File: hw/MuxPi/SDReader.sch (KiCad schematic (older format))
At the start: 32 parts, among them IC1 AT24C02D-SSHM-T, P17 USBA-2G, U9 USB2640-HZH-02, Y2 LF XTAL012504 - 24MHz

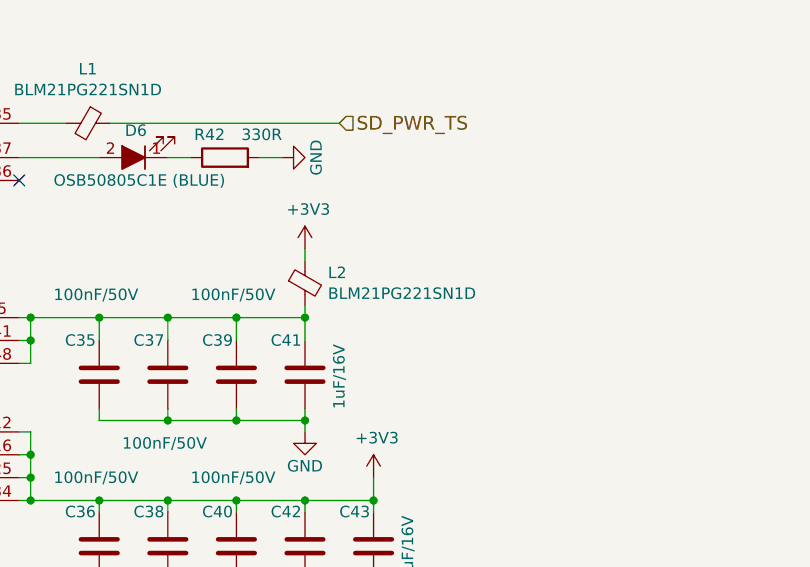
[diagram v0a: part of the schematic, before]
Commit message: Add detailed info to MuxPi electronic components
The additional information includes manufacturer names and
manufacturer symbols for all components except ceramic capacitors
and resistors. It allows to create BOM (Bill Of Materials) with
actual product names.

Change-Id: Id1c518bba60322d4b8b132ad14261806070abc27
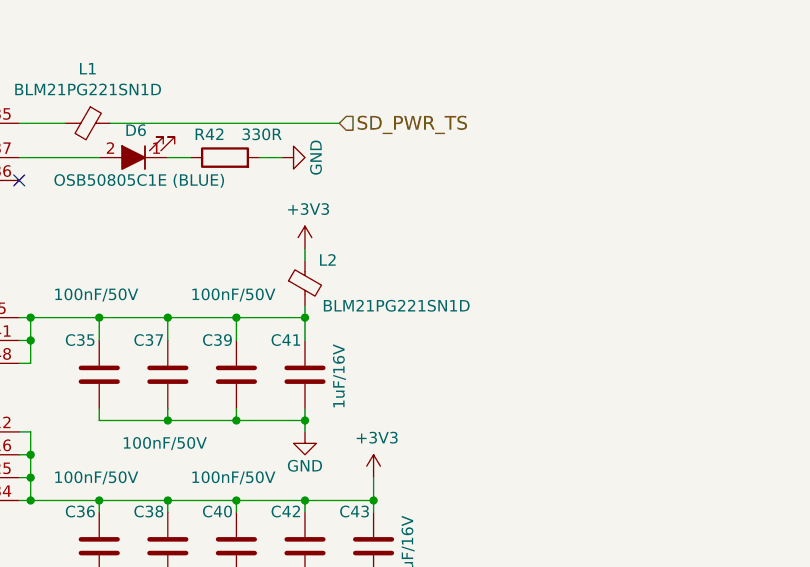
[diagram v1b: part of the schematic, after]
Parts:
- D6: Manufacturer (none) -> OPTOSUPPLY; Symbol (none) -> OSB50805C1E
- IC1: Manufacturer (none) -> MICROCHIP (ATMEL); Symbol (none) -> AT24C02D-SSHM-T
- L1, L2: Manufacturer (none) -> MURATA; Symbol (none) -> BLM21PG221SN1D
- P17: Manufacturer (none) -> CONNFLY; Symbol (none) -> DS1096-BN0
- U9: Manufacturer (none) -> MICROCHIP; Symbol (none) -> USB2640-HZH-02
- Y2: Manufacturer (none) -> IQD FREQUENCY PRODUCTS; Symbol (none) -> LF XTAL012504
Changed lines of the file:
@@
 F 3 "http://www.farnell.com/datasheets/2138035.pdf?_ga=1.187806955.291132730.1474618953" H 7450 2500 50  0001 C CNN
 F 4 "http://pl.farnell.com/microchip/usb2640-hzh-02/ic-usb-2-flash-media-cntrl-48vqfn/dp/2292611" H 5500 2400 60  0001 C CNN "Shop link"
+F 5 "USB2640-HZH-02" H 5500 2400 50  0001 C CNN "Symbol"
+F 6 "MICROCHIP" H 5500 2400 50  0001 C CNN "Manufacturer"
 	1    5500 2400
 	1    0    0    -1
@@
 F 3 "http://www.farnell.com/datasheets/2138035.pdf?_ga=1.187806955.291132730.1474618953" H 5250 6050 50  0001 C CNN
 F 4 "http://pl.farnell.com/microchip/usb2640-hzh-02/ic-usb-2-flash-media-cntrl-48vqfn/dp/2292611" H 3300 5950 60  0001 C CNN "Shop link"
+F 5 "MICROCHIP" H 3300 5950 50  0001 C CNN "Manufacturer"
+F 6 "USB2640-HZH-02" H 3300 5950 50  0001 C CNN "Symbol"
 	2    3300 5950
 	1    0    0    -1
@@
 F 3 "http://www.tme.eu/pl/Document/9ec5256b58bf67caf05d35a0814832e6/AT24C01D-MAHM-T.pdf" H 3650 3600 50  0001 C CNN
 F 4 "http://www.tme.eu/pl/details/at24c02d-sshm-t/pamieci-eeprom-szeregowe/atmel/" H 3650 3600 60  0001 C CNN "Shop link"
+F 5 "MICROCHIP (ATMEL)" H 3650 3600 50  0001 C CNN "Manufacturer"
+F 6 "AT24C02D-SSHM-T" H 3650 3600 50  0001 C CNN "Symbol"
 	1    3650 3600
 	1    0    0    -1
@@
 F 3 "http://www.tme.eu/pl/Document/fd32e3a1954dc23b6c626158f627af96/hc49_4hsmx.pdf" H 1750 5550 50  0001 C CNN
 F 4 "http://www.tme.eu/pl/details/24.00m-smdhc49r/rezonatory-kwarcowe-smd/iqd-frequency-products/lf-xtal012504/" V 1750 5550 60  0001 C CNN "Shop link"
+F 5 "IQD FREQUENCY PRODUCTS" V 1750 5550 50  0001 C CNN "Manufacturer"
+F 6 "LF XTAL012504" V 1750 5550 50  0001 C CNN "Symbol"
 	1    1750 5550
 	0    1    1    0
@@
 $EndComp
 $Comp
-L MuxPi:Ferrite_Bead_Small L2
-U 1 1 5846AD7D
-P 5350 5900
-F 0 "L2" H 5450 5946 50  0000 L CNN
-F 1 "BLM21PG221SN1D" H 5450 5855 50  0000 L CNN
-F 2 "Resistors_SMD:R_0805_HandSoldering" H 5450 5809 50  0001 L CNN
-F 3 "http://www.tme.eu/pl/Document/6052c7f9d4f1672121538e0d10f79ff8/blm21pg300sn1d.pdf" H 5450 5809 50  0001 L CNN
-F 4 "http://www.tme.eu/pl/details/blm21pg221sn1d/ferryty-koraliki/murata/" H 5350 5900 60  0001 C CNN "Shop link"
-	1    5350 5900
-	1    0    0    -1
-$EndComp
-$Comp
 L MuxPi:+3V3 #PWR0129
 U 1 1 5846B688
@@
 F 3 "http://www.tme.eu/pl/Document/6052c7f9d4f1672121538e0d10f79ff8/blm21pg300sn1d.pdf" H 4500 5109 50  0001 L CNN
 F 4 "http://www.tme.eu/pl/details/blm21pg221sn1d/ferryty-koraliki/murata/" H 4400 5200 60  0001 C CNN "Shop link"
+F 5 "MURATA" V 4400 5200 50  0001 C CNN "Manufacturer"
+F 6 "BLM21PG221SN1D" V 4400 5200 50  0001 C CNN "Symbol"
 	1    4400 5200
 	0    1    1    0
@@
 F 3 "http://www.tme.eu/pl/Document/7923e8726ae07a0825304f6fd9a186c2/usba-2g.pdf" V 10350 1300 50  0001 C CNN
 F 4 "http://www.tme.eu/pl/details/usba-2g/zlacza-usb-i-ieee1394/ninigi/" V 10400 1400 60  0001 C CNN "Shop link"
+F 5 "CONNFLY" V 10400 1400 50  0001 C CNN "Manufacturer"
+F 6 "DS1096-BN0" V 10400 1400 50  0001 C CNN "Symbol"
 	1    10400 1400
 	0    1    1    0
@@
 F 3 "http://www.tme.eu/pl/Document/6f99baddc8b38eb1a865ea6b78250b2b/OSXX0805C1E-DTE.pdf" H 4600 5350 50  0001 C CNN
 F 4 "http://www.tme.eu/pl/details/osb50805c1e/diody-led-smd-kolorowe/optosupply/" V 4600 5350 60  0001 C CNN "Shop link"
+F 5 "OPTOSUPPLY" H 4600 5350 50  0001 C CNN "Manufacturer"
+F 6 "OSB50805C1E" H 4600 5350 50  0001 C CNN "Symbol"
 	1    4600 5350
 	-1   0    0    1
@@
 Wire Wire Line
 	1450 5800 1750 5800
+$Comp
+L MuxPi:Ferrite_Bead_Small L2
+U 1 1 5A8DBC88
+P 5350 5900
+F 0 "L2" H 5450 6000 50  0000 C CNN
+F 1 "BLM21PG221SN1D" H 5750 5800 50  0000 C CNN
+F 2 "Resistors_SMD:R_0805_HandSoldering" H 5450 5809 50  0001 L CNN
+F 3 "http://www.tme.eu/pl/Document/6052c7f9d4f1672121538e0d10f79ff8/blm21pg300sn1d.pdf" H 5450 5809 50  0001 L CNN
+F 4 "http://www.tme.eu/pl/details/blm21pg221sn1d/ferryty-koraliki/murata/" H 5350 5900 60  0001 C CNN "Shop link"
+F 5 "MURATA" V 5350 5900 50  0001 C CNN "Manufacturer"
+F 6 "BLM21PG221SN1D" V 5350 5900 50  0001 C CNN "Symbol"
+	1    5350 5900
+	1    0    0    -1
+$EndComp
 $EndSCHEMATC

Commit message: Update hardware design to version 1.3
Change-Id: I17b3f32943a6fd048f05d1b0d8676607dc54b976
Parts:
- L1, L2: footprint Resistors_SMD:R_0805_HandSoldering -> Resistors_SMD:R_0805
- R42: value 330R -> 560R; Shop link http://www.tme.eu/pl/details/rc0805jr-07330r/rezystory-smd-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 -> (none)
- R43: value 330R -> 10K; Shop link http://www.tme.eu/pl/details/rc0805jr-07330r/rezystory-smd-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 -> (none)
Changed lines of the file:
@@
 Sheet 9 12
 Title "MuxPi"
-Date "2018-04-20"
-Rev "1.2"
+Date "2018-08-14"
+Rev "1.3"
 Comp "SRPOL"
 Comment1 "Author: Adam Malinowski <a.malinowsk2@partner.samsung.com>"
-Comment2 "Copyright (c) 2016 - 2018 Samsung Electronics Co., Ltd All Rights Reserved"
+Comment2 "Copyright (c) 2016 -2018 Samsung Electronics Co., Ltd All Rights Reserved"
 Comment3 ""
 Comment4 ""
@@
 F 0 "L1" V 4163 5200 50  0000 C CNN
 F 1 "BLM21PG221SN1D" V 4254 5200 50  0000 C CNN
-F 2 "Resistors_SMD:R_0805_HandSoldering" H 4500 5109 50  0001 L CNN
+F 2 "Resistors_SMD:R_0805" H 4500 5109 50  0001 L CNN
 F 3 "http://www.tme.eu/pl/Document/6052c7f9d4f1672121538e0d10f79ff8/blm21pg300sn1d.pdf" H 4500 5109 50  0001 L CNN
 F 4 "http://www.tme.eu/pl/details/blm21pg221sn1d/ferryty-koraliki/murata/" H 4400 5200 60  0001 C CNN "Shop link"
@@
 P 5000 5350
 F 0 "R42" V 5100 5350 50  0000 L CNN
-F 1 "330R" V 5100 5100 50  0000 L CNN
+F 1 "560R" V 5100 5100 50  0000 L CNN
 F 2 "Resistors_SMD:R_0805" V 4930 5350 50  0001 C CNN
 F 3 "http://www.tme.eu/pl/Document/7b8fed8c112f8a94930279c22c957f7f/rc0805yageo.pdf" H 5000 5350 50  0001 C CNN
-F 4 "http://www.tme.eu/pl/details/rc0805jr-07330r/rezystory-smd-0805/yageo/rc0805jr-07330rl/" V 5000 5350 60  0001 C CNN "Shop link"
 	1    5000 5350
 	0    -1   -1   0
@@
 P 10600 2350
 F 0 "R43" H 10650 2450 50  0000 L CNN
-F 1 "330R" H 10650 2350 50  0000 L CNN
+F 1 "10K" H 10650 2350 50  0000 L CNN
 F 2 "Resistors_SMD:R_0805" V 10530 2350 50  0001 C CNN
 F 3 "http://www.tme.eu/pl/Document/7b8fed8c112f8a94930279c22c957f7f/rc0805yageo.pdf" H 10600 2350 50  0001 C CNN
-F 4 "http://www.tme.eu/pl/details/rc0805jr-07330r/rezystory-smd-0805/yageo/rc0805jr-07330rl/" V 10600 2350 60  0001 C CNN "Shop link"
 	1    10600 2350
 	1    0    0    -1
@@
 F 0 "L2" H 5450 6000 50  0000 C CNN
 F 1 "BLM21PG221SN1D" H 5750 5800 50  0000 C CNN
-F 2 "Resistors_SMD:R_0805_HandSoldering" H 5450 5809 50  0001 L CNN
+F 2 "Resistors_SMD:R_0805" H 5450 5809 50  0001 L CNN
 F 3 "http://www.tme.eu/pl/Document/6052c7f9d4f1672121538e0d10f79ff8/blm21pg300sn1d.pdf" H 5450 5809 50  0001 L CNN
 F 4 "http://www.tme.eu/pl/details/blm21pg221sn1d/ferryty-koraliki/murata/" H 5350 5900 60  0001 C CNN "Shop link"

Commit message: Update  hardware design to version 1.4
Change-Id: I72a4381d8bec5616bc1cfe04dc8a5407141c77d5
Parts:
- removed Y2: LF XTAL012504 - 24MHz, Crystals:Q_49U3HMS, symbol MuxPi:Crystal
- added Y2: LF XTAL012504 - 24MHz, Crystal:Crystal_SMD_2520-4Pin_2.5x2.0mm, symbol Device:Crystal_GND24
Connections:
- net GND: now also Y2.2, Y2.4
- net at C29.1, R37.2, U9.45 (XTAL1/CLKIN): now also Y2.1
- net at C30.1, R37.1, U9.44 (XTAL2): now also Y2.3
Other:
- moved on the sheet: R37
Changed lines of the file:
@@
 EESchema Schematic File Version 4
 LIBS:MuxPi-cache
-EELAYER 26 0
+EELAYER 29 0
 EELAYER END
 $Descr A4 11693 8268
@@
 Sheet 9 12
 Title "MuxPi"
-Date "2018-08-14"
-Rev "1.3"
+Date "2018-11-16"
+Rev "1.4"
 Comp "SRPOL"
 Comment1 "Author: Adam Malinowski <a.malinowsk2@partner.samsung.com>"
@@
 $EndComp
 $Comp
-L MuxPi:Crystal Y2
-U 1 1 584578D0
-P 1750 5550
-F 0 "Y2" V 1600 5450 50  0000 C CNN
-F 1 "LF XTAL012504 - 24MHz" V 1350 5800 50  0000 C CNN
-F 2 "Crystals:Q_49U3HMS" H 1750 5550 50  0001 C CNN
-F 3 "http://www.tme.eu/pl/Document/fd32e3a1954dc23b6c626158f627af96/hc49_4hsmx.pdf" H 1750 5550 50  0001 C CNN
-F 4 "http://www.tme.eu/pl/details/24.00m-smdhc49r/rezonatory-kwarcowe-smd/iqd-frequency-products/lf-xtal012504/" V 1750 5550 60  0001 C CNN "Shop link"
-F 5 "IQD FREQUENCY PRODUCTS" V 1750 5550 50  0001 C CNN "Manufacturer"
-F 6 "LF XTAL012504" V 1750 5550 50  0001 C CNN "Symbol"
-	1    1750 5550
-	0    1    1    0
-$EndComp
-$Comp
 L MuxPi:GND #PWR0121
 U 1 1 584578D7
@@
 	2150 5750 2100 5750
 Wire Wire Line
-	2100 5350 2100 5750
+	2100 5350 2100 5550
 Wire Wire Line
 	850  5800 950  5800
@@
 	850  5300 950  5300
 Wire Wire Line
-	1250 5300 1450 5300
-Wire Wire Line
-	1250 5800 1450 5800
+	1250 5300 1350 5300
+Wire Wire Line
+	1250 5800 1350 5800
 Wire Wire Line
 	1750 5400 1750 5300
@@
 Connection ~ 1750 5800
 Wire Wire Line
-	2500 5500 1950 5500
-Wire Wire Line
-	1950 5500 1950 5300
-Wire Wire Line
-	2500 5600 1950 5600
-Wire Wire Line
-	1950 5600 1950 5800
+	2500 5500 2000 5500
+Wire Wire Line
+	2000 5500 2000 5300
+Wire Wire Line
+	2500 5600 2000 5600
+Wire Wire Line
+	2000 5600 2000 5800
 Wire Wire Line
 	850  4900 850  5300
@@
 L MuxPi:R R37
 U 1 1 58525399
-P 1450 5550
-F 0 "R37" H 1350 5600 50  0000 C CNN
-F 1 "1M" H 1350 5700 50  0000 C CNN
-F 2 "Resistors_SMD:R_0805" V 1380 5550 30  0001 C CNN
-F 3 "http://www.tme.eu/pl/Document/393e95a6d9f61f4002588a56cd2a1091/rezystor-smd.pdf" H 1450 5550 30  0001 C CNN
-F 4 "http://www.tme.eu/pl/details/smd0805-1m/rezystory-smd-0805/royal-ohm/0805s8j0105t5e/" V 1450 5550 60  0001 C CNN "Shop link"
-	1    1450 5550
+P 1350 5550
+F 0 "R37" H 1250 5400 50  0000 C CNN
+F 1 "1M" H 1250 5500 50  0000 C CNN
+F 2 "Resistors_SMD:R_0805" V 1280 5550 30  0001 C CNN
+F 3 "http://www.tme.eu/pl/Document/393e95a6d9f61f4002588a56cd2a1091/rezystor-smd.pdf" H 1350 5550 30  0001 C CNN
+F 4 "http://www.tme.eu/pl/details/smd0805-1m/rezystory-smd-0805/royal-ohm/0805s8j0105t5e/" V 1350 5550 60  0001 C CNN "Shop link"
+	1    1350 5550
 	-1   0    0    1
 $EndComp
 Wire Wire Line
-	1450 5400 1450 5300
-Connection ~ 1450 5300
-Wire Wire Line
-	1450 5700 1450 5800
-Connection ~ 1450 5800
+	1350 5400 1350 5300
+Connection ~ 1350 5300
+Wire Wire Line
+	1350 5700 1350 5800
+Connection ~ 1350 5800
 Wire Wire Line
 	10050 1600 10100 1600
@@
 	1300 4900 1350 4900
 Wire Wire Line
-	1750 5300 1950 5300
-Wire Wire Line
-	1750 5800 1950 5800
+	1750 5300 2000 5300
+Wire Wire Line
+	1750 5800 2000 5800
 Wire Wire Line
 	850  5800 850  5900
@@
 	10000 1900 10000 1950
 Wire Wire Line
-	1450 5300 1750 5300
-Wire Wire Line
-	1450 5800 1750 5800
+	1350 5300 1750 5300
+Wire Wire Line
+	1350 5800 1750 5800
 $Comp
 L MuxPi:Ferrite_Bead_Small L2
@@
 	1    0    0    -1
 $EndComp
+$Comp
+L Device:Crystal_GND24 Y2
+U 1 1 5BF160EA
+P 1750 5550
+F 0 "Y2" V 1550 5600 50  0000 L CNN
+F 1 "LF XTAL012504 - 24MHz" V 1350 5200 50  0000 L CNN
+F 2 "Crystal:Crystal_SMD_2520-4Pin_2.5x2.0mm" H 1750 5550 50  0001 C CNN
+F 3 "http://www.tme.eu/pl/Document/43d4b8b2418f10b1847f5f6593a9a63f/cfpx-218.pdf" H 1750 5550 50  0001 C CNN
+F 4 "http://www.tme.eu/pl/details/24.00m-cfpx218/rezonatory-kwarcowe-smd/iqd-frequency-products/lfxtal053106bulk/" H 1750 5550 50  0001 C CNN "Shop link"
+F 5 "IQD FREQUENCY PRODUCTS" H 1750 5550 50  0001 C CNN "Manufacturer"
+F 6 "LFXTAL053106BULK" H 1750 5550 50  0001 C CNN "Symbol"
+	1    1750 5550
+	0    1    1    0
+$EndComp
+Wire Wire Line
+	1950 5550 2100 5550
+Connection ~ 2100 5550
+Wire Wire Line
+	2100 5550 2100 5750
+$Comp
+L MuxPi:GND #PWR0197
+U 1 1 5BF40C91
+P 1500 5850
+F 0 "#PWR0197" H 1500 5600 50  0001 C CNN
+F 1 "GND" H 1500 5700 50  0000 C CNN
+F 2 "" H 1500 5850 60  0000 C CNN
+F 3 "" H 1500 5850 60  0000 C CNN
+	1    1500 5850
+	-1   0    0    -1
+$EndComp
+Wire Wire Line
+	1500 5850 1500 5550
+Wire Wire Line
+	1500 5550 1550 5550
 $EndSCHEMATC
